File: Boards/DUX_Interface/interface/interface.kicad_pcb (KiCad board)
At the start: 2 copper layers, 208.5 x 42.1 mm, 14 parts, among them J1 MM_F_VT_20, J2 MM_F_VT_20, J3 MM_F_VT_04, J4 MM_F_VT_10, J5 MM_F_VT_04, J6 NF_F_RA_2x02, J7 Ampseal_35_VT, J8 MicroFit_RA_V_2, U1 Nanofit_12, U2 Nanofit_4, U3 Nanofit_4, U4 Nanofit_10, U5 RJ45_VT, U6 RJ45_VT

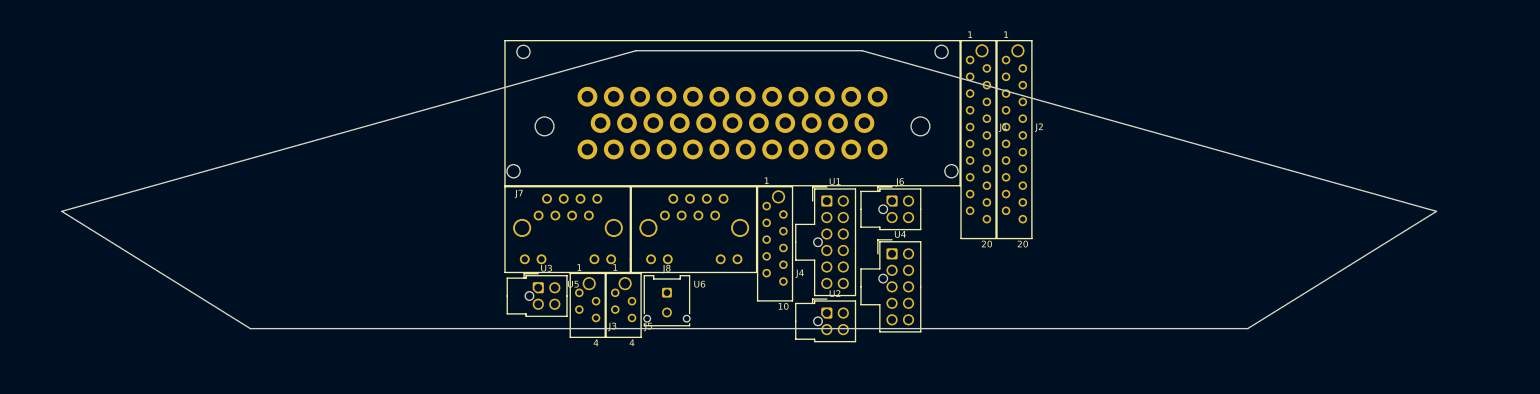
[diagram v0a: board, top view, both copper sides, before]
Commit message: Initial placement of dash interface board connectors
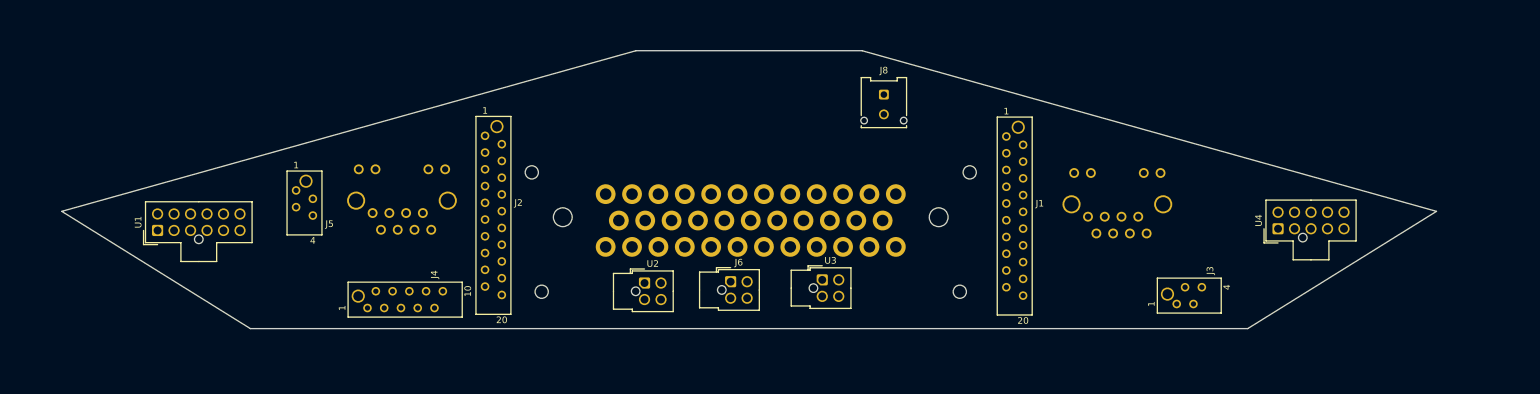
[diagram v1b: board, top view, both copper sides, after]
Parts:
- J7, U5, U6: moved to B.Cu
- moved U1 101.6 mm to (61.3, 81.3), turned to 90 degrees
- moved J3 95.7 mm to (221.0, 92.5), turned to 90 degrees
- moved U5 84.3 mm to (200.3, 72.6)
- moved J2 79.8 mm to (111.0, 72.1)
- moved U4 58.7 mm to (231.2, 81.1), turned to 90 degrees
- moved J4 56.7 mm to (98.9, 91.8), turned to 90 degrees
- moved J5 50.8 mm to (82.3, 80.3)
- moved U6 46.4 mm to (91.8, 72.1)
- moved J8 44.5 mm to (171.5, 60.7)
- moved U3 43.1 mm to (162.1, 88.8)
- moved U2 28.0 mm to (135.2, 89.3)
- moved J6 27.4 mm to (148.2, 89.1)
- moved J7 14.0 mm to (122.8, 79.3)
- moved J1 12.8 mm to (190.0, 72.2)

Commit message: Exported preliminary layout as step file; almost finished layout
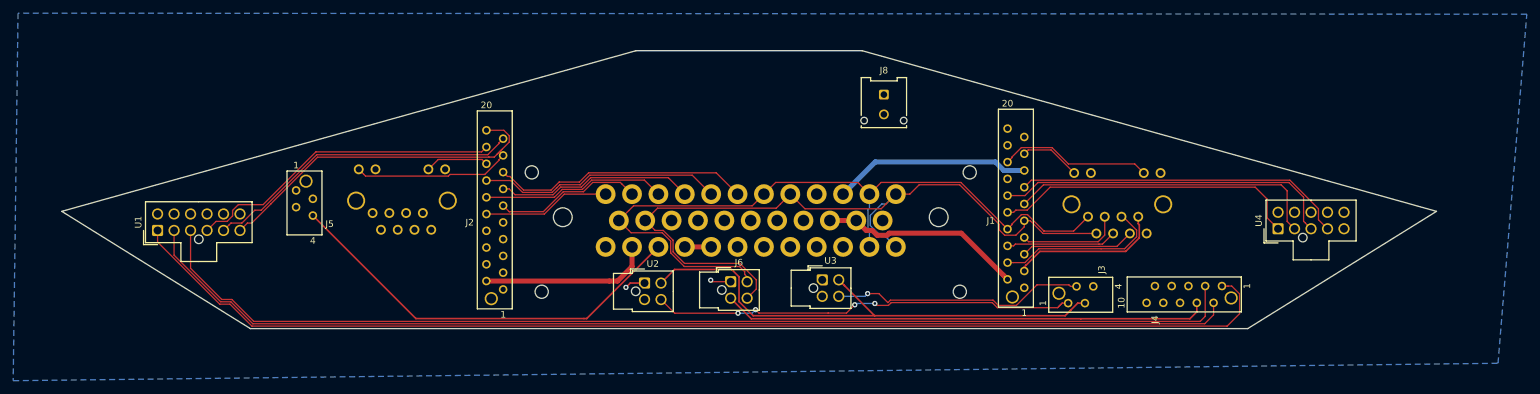
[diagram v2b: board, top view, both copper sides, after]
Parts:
- moved J4 118.1 mm to (217.0, 91.0), turned to 270 degrees
- moved J3 16.5 mm to (204.5, 92.4)
- moved J2 13.4 mm to (113.7, 85.2), turned to 180 degrees
- moved J1 13.1 mm to (192.8, 84.9), turned to 180 degrees
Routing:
- net /LV_LED: track 0.00 -> 178.0 mm
- net /HV_LED: track 0.00 -> 168.1 mm
- net /BRAKE_LED: track 0.00 -> 167.8 mm
- net /CANL: track 0.00 -> 116.7 mm
- net /CANH: track 0.00 -> 114.1 mm
- net /5V_LED_BARS: track 0.00 -> 78.7 mm
- net /5V_STEERING: track 0.00 -> 73.8 mm
- net /SPEED_LED_BAR: track 0.00 -> 65.5 mm, vias 0 -> 4
- net /5V_CAN_LOGGER: track 0.00 -> 63.4 mm
- net +12V: track 0.00 -> 57.8 mm
- net /DRIVE_MODE_-: track 0.00 -> 52.2 mm
- net /BMS_LED: track 0.00 -> 51.9 mm
- net /IMD_LED: track 0.00 -> 50.5 mm
- net /DRIVE_MODE_SENSE: track 0.00 -> 48.2 mm
- net /DRIVE_MODE_+: track 0.00 -> 48.1 mm
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- added copper zone on B.Cu, net GND
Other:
- rule trace_min: 0.2 -> 0.1524

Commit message: Almost done with dash interface rev0
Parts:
- moved U1 86.5 mm to (146.1, 64.1), turned to 270 degrees
- moved U4 75.8 mm to (156.8, 66.6)
- moved J8 31.8 mm to (158.8, 89.8), turned to 90 degrees
- moved U6 20.6 mm to (104.1, 88.6), turned to 180 degrees
- moved U3 12.3 mm to (174.4, 89.0)
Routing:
- net +12V: track 57.8 -> 144.9 mm
- net /LV_LED: track 178.0 -> 102.3 mm
- net /STEERING_POT_+: track 0.00 -> 74.1 mm, vias 0 -> 1
- net /STEERING_POT_SENSE: track 0.00 -> 66.2 mm, vias 0 -> 1
- net /STEERING_POT_-: track 0.00 -> 62.8 mm, vias 0 -> 1
- net /HV_LED: track 168.1 -> 108.2 mm
- net /BRAKE_LED: track 167.8 -> 111.3 mm
- net /CANL: track 116.7 -> 151.5 mm
- net /CANH: track 114.1 -> 147.0 mm
- net /RJ45_LED_G_THROTTLE: track 23.7 -> 53.0 mm
- net /DRIVE_MODE_-: track 52.2 -> 23.2 mm
- net /RJ45_LED_O_THROTTLE: track 9.68 -> 35.9 mm
- net /DRIVE_MODE_SENSE: track 48.2 -> 24.3 mm
- net /MOSI_THROTTLE: track 0.00 -> 23.2 mm
- net /5V_THROTTLE: track 0.00 -> 21.8 mm
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
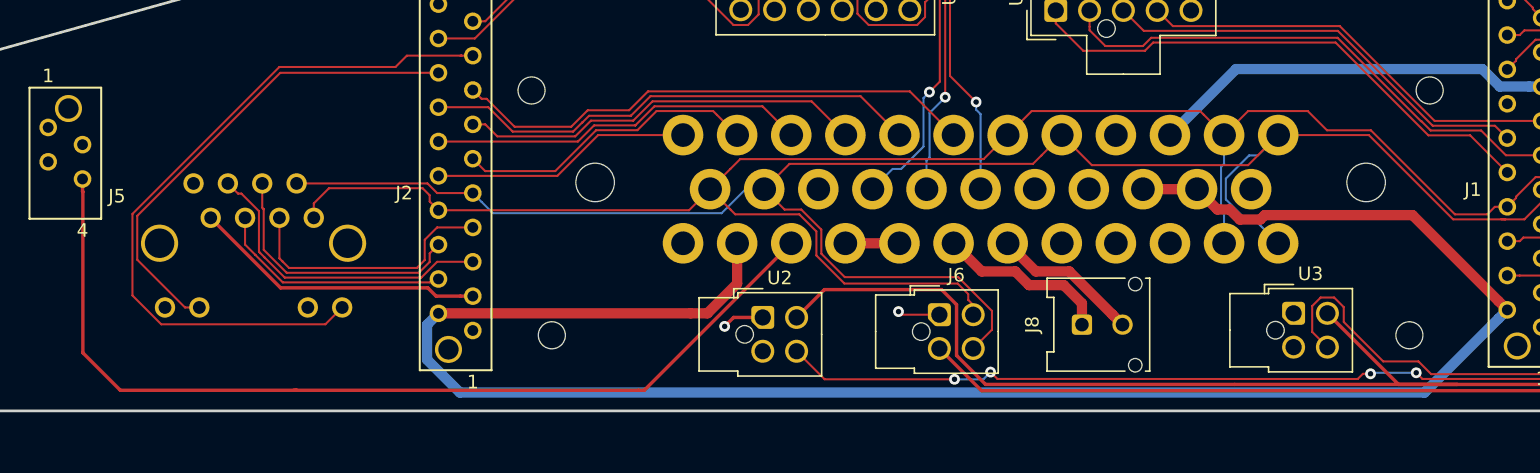
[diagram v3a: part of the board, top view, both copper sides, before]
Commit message: Reassigned nanofits to new parts; cleaned up layout a bit
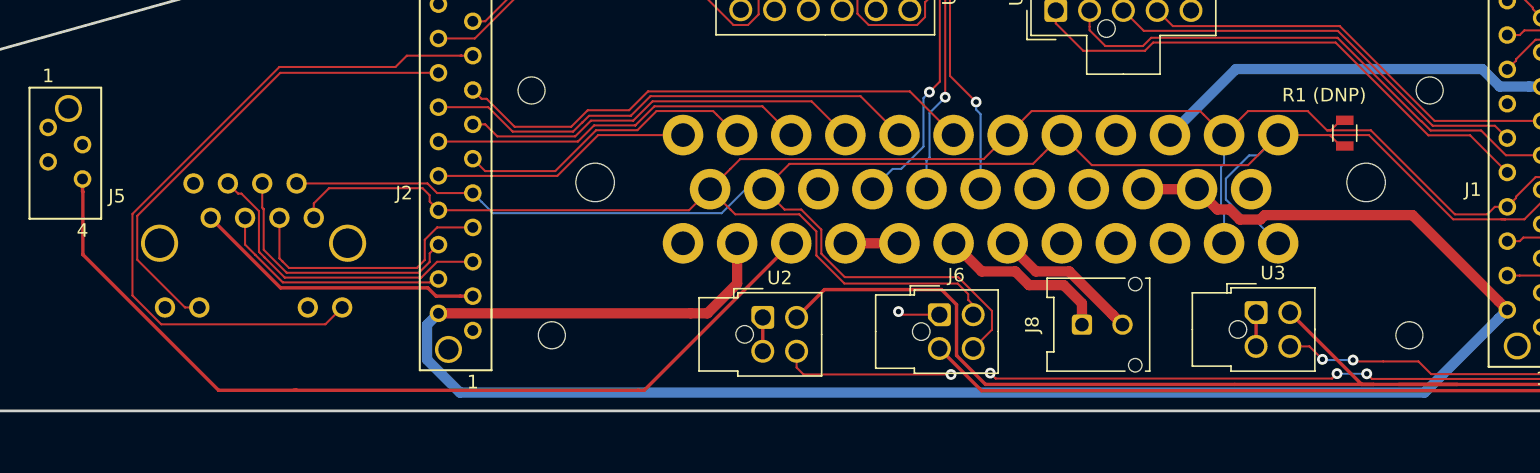
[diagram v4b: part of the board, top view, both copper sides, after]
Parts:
- added R1 (DNP): R_120_DNP, footprints:R_0805_OEM, F.Cu at (178.2, 75.7)
- moved U3 2.78 mm to (171.6, 88.9)
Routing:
- net /SOC_LED_BAR: track 34.8 -> 30.6 mm, vias 0 -> 2
- net /5V_CAN_LOGGER: track 71.1 -> 66.8 mm
- net GND: track 6.21 -> 8.12 mm, vias 2 -> 1
- net /CANH: track 147.0 -> 148.6 mm
- net /CANL: track 151.5 -> 153.0 mm
- net /5V_LED_BARS: track 82.8 -> 83.8 mm

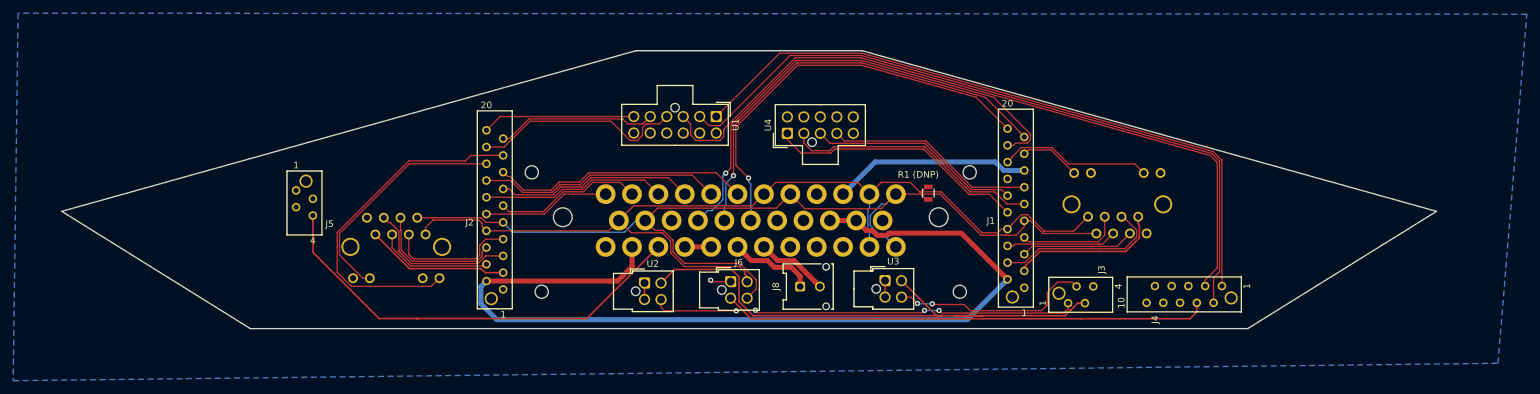
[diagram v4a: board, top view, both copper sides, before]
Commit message: final connector placement for dux interface rev1
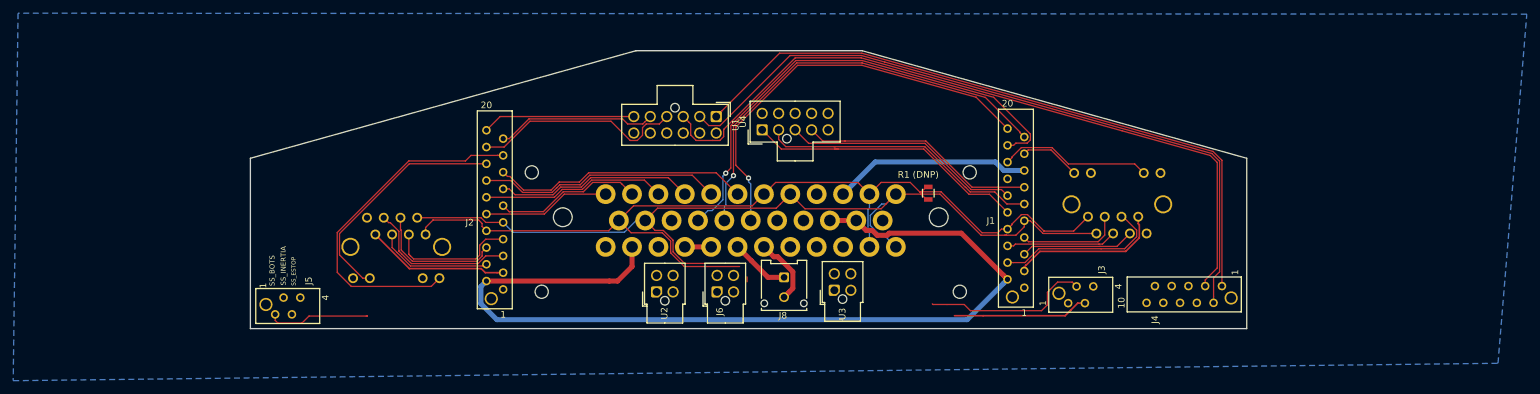
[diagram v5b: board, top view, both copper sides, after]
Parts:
- moved J5 13.8 mm to (84.3, 94.1), turned to 90 degrees
- moved U3 7.83 mm to (164.0, 90.4), turned to 90 degrees
- moved U4 3.86 mm to (153.0, 66.1)
- moved J8 2.81 mm to (156.3, 88.4), turned to 0 degrees
- moved J6 2.58 mm to (146.2, 90.7), turned to 90 degrees
- moved U2 2.27 mm to (137.0, 90.7), turned to 90 degrees
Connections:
- J5 pad 1: /SS_BOTS -> /BOTS>ESTOP
- J5 pad 2: /SS_INERTIA -> /IS>BOTS
- J5 pad 3: /SS_ESTOP -> /ESTOP>HVD
- J7 pad 19: /5V_DUX -> GND
- J7 pad 9: /5V_THROTTLE -> GND
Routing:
- net /5V_STEERING: track 73.8 -> 0.00 mm
- net /5V_CAN_LOGGER: track 66.8 -> 0.00 mm
- net /SPEED_LED_BAR: track 65.0 -> 0.00 mm, vias 4 -> 0
- net /5V_LED_BARS: track 83.8 -> 20.6 mm
- net /BOTS>ESTOP: track 12.9 -> 24.6 mm
- net GND: track 8.12 -> 0.16 mm, vias 1 -> 0
- net /CANL: track 153.0 -> 146.8 mm
- net /SOC_LED_BAR: track 30.6 -> 25.5 mm, vias 2 -> 0
- net /IMD_LED: track 31.8 -> 35.9 mm
- net /BMS_LED: track 32.3 -> 36.3 mm
- net /START_LED: track 39.2 -> 42.9 mm
- net /START_BTN: track 39.4 -> 42.8 mm
- net /CANH: track 148.6 -> 145.8 mm
- net /ESTOP>HVD: track 11.0 -> 10.3 mm
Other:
- board size 208.5 x 42.1 mm -> 151.1 x 42.1 mm
- board text added: "SS_BOTS"
- board text added: "SS_ESTOP"
- board text added: "SS_INERTIA"

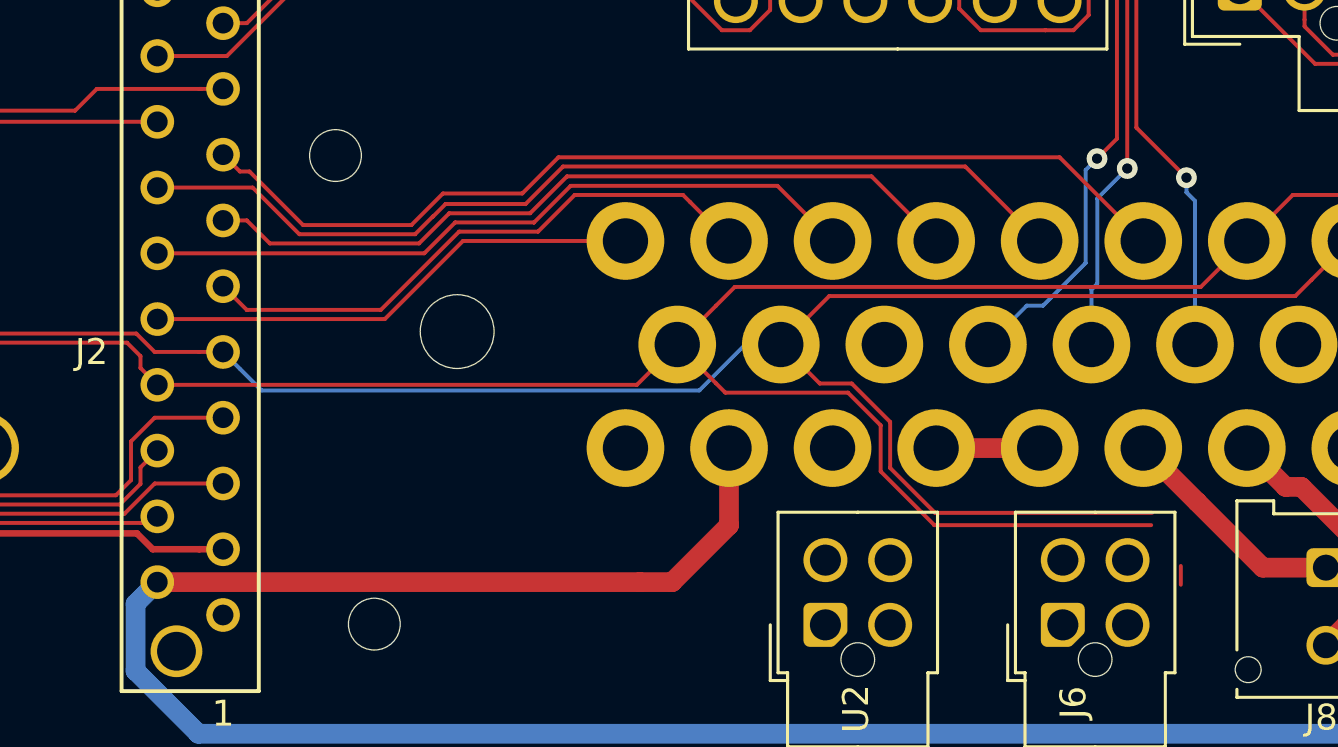
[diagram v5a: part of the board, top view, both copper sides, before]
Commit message: Working on moving nanofits on REV1 interface board
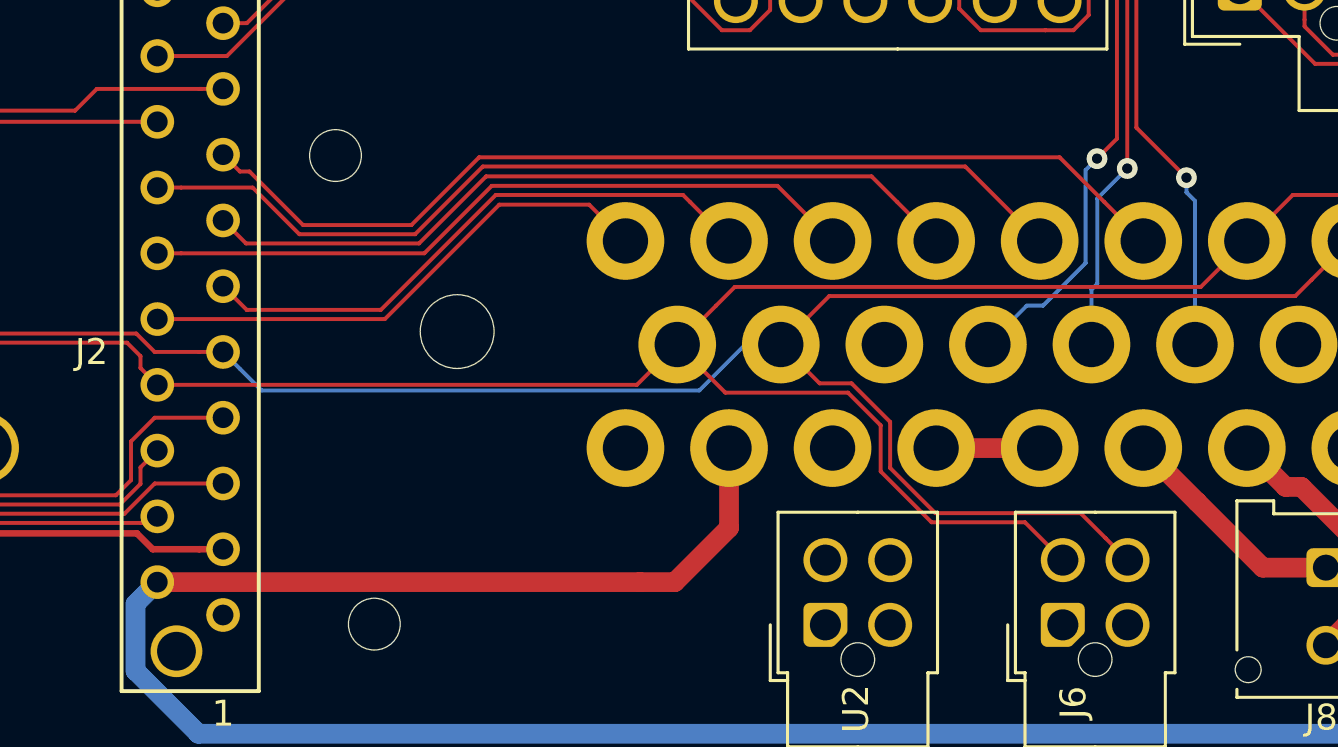
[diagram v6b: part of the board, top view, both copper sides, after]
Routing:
- net /CANH: track 145.8 -> 143.0 mm
- net /THROTTLE_POT_1_+: track 19.3 -> 20.5 mm
- net /CANL: track 146.8 -> 145.9 mm

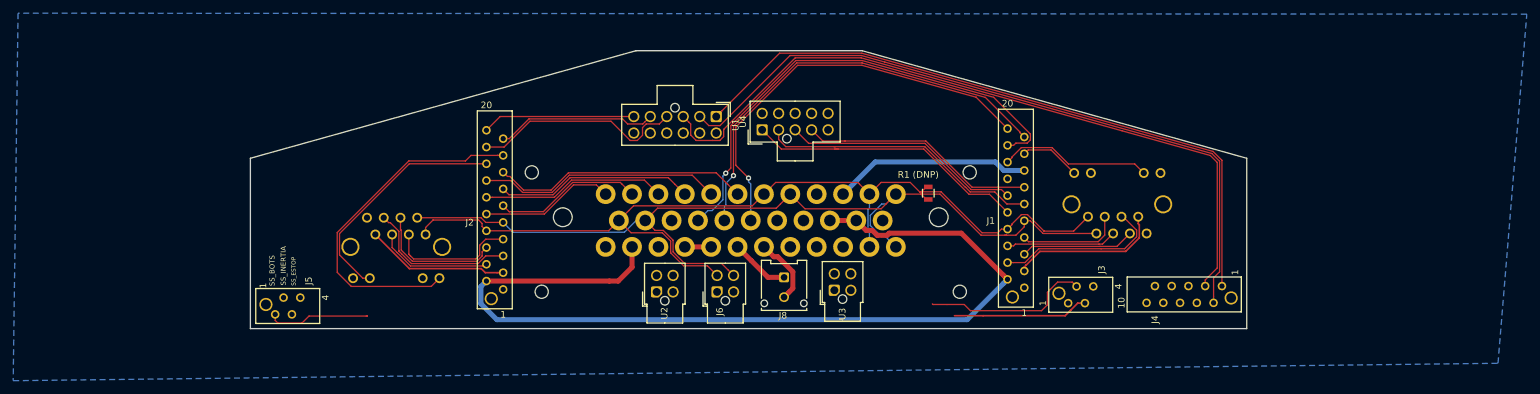
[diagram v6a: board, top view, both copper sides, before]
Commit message: Re-traced lines to repositioned connectors; now all finger-tabs face outwards
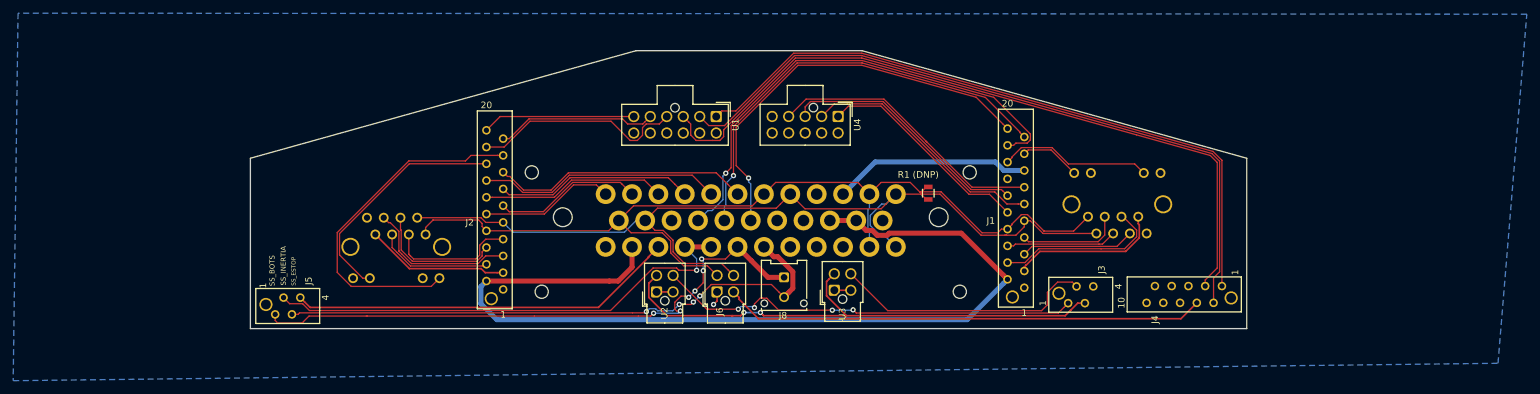
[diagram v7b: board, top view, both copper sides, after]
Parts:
- moved U4 11.7 mm to (164.5, 64.0), turned to 270 degrees
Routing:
- net /ESTOP>HVD: track 10.3 -> 87.9 mm, vias 0 -> 4
- net /5V_STEERING: track 0.00 -> 73.1 mm
- net /IS>BOTS: track 4.00 -> 74.5 mm, vias 0 -> 1
- net /BOTS>ESTOP: track 24.6 -> 90.0 mm, vias 0 -> 6
- net /SPEED_LED_BAR: track 0.00 -> 64.9 mm, vias 0 -> 4
- net /5V_LED_BARS: track 20.6 -> 80.5 mm, vias 0 -> 2
- net /5V_CAN_LOGGER: track 0.00 -> 58.8 mm
- net /SOC_LED_BAR: track 25.5 -> 39.7 mm
- net /START_BTN: track 42.8 -> 33.0 mm
- net GND: track 0.16 -> 7.29 mm, vias 0 -> 1
- net /IMD_LED: track 35.9 -> 42.5 mm
- net /START_LED: track 42.9 -> 37.8 mm
- net /BMS_LED: track 36.3 -> 38.4 mm
